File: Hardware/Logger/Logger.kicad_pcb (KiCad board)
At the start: 2 copper layers, 70 x 71 mm, 93 parts, among them CN1 Conn_02x19_Odd_Even, CN10 Conn_02x19_Odd_Even, CN2 Conn_02x19_Odd_Even, CN7 Conn_02x19_Odd_Even, J1 Conn_Coaxial, J10 Conn_01x08_Female, J2 Conn_Coaxial, J3 Conn_Coaxial, J4 Conn_Coaxial, J5 USB_B_Micro, J6 112K-TAA0-RA1_ATTEND, J7 DB9_Female_MountingHoles, J8 Conn_01x06_Female, J9 Conn_01x08_Female, Q1 FDV304P, Q2 FDV304P, Q3 FDV304P, Q4 FDV304P, Q5 BC848, Q6 BC848, Q7 BC848, Q8 BC848, SW1 SW_Push, SW2 SW_Push, SW3 SW_Push, SW4 SW_Push, U1 ESP-12E, U2 ST7735S, U3 LD1117ASTR

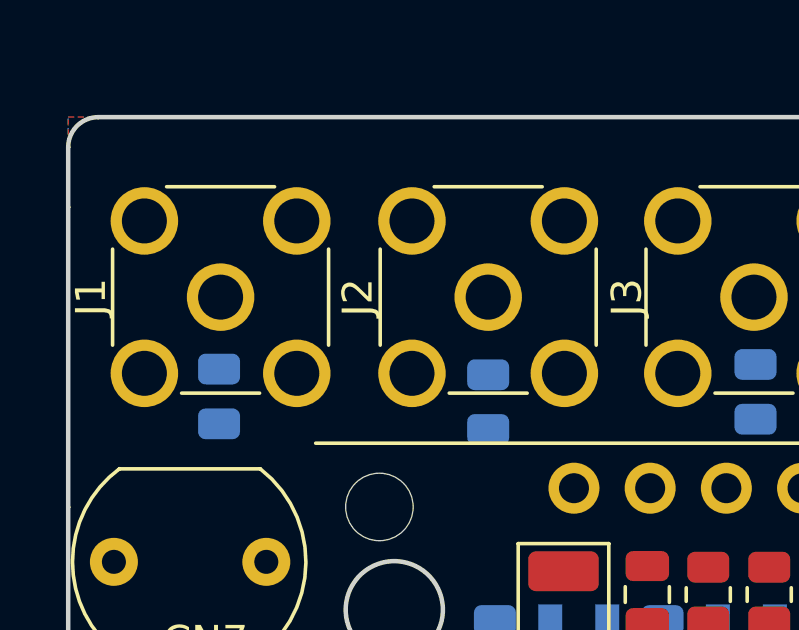
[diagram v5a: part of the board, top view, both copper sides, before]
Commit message: cleanup after transition to KiCad6
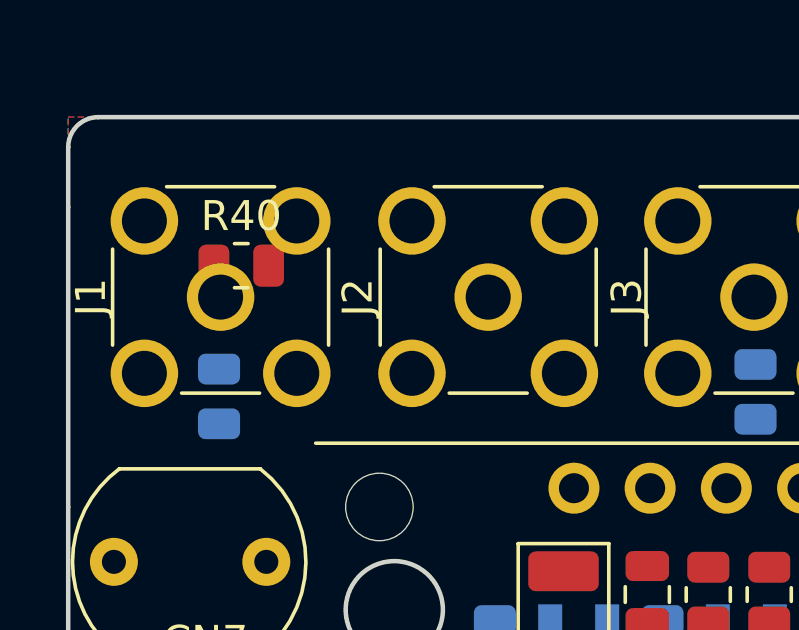
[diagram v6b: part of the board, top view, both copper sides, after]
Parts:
- removed the R10 at (144.0, 60.5)
- added R40: 100R, Resistor_SMD:R_0805_2012Metric, F.Cu at (135.8, 56.0)

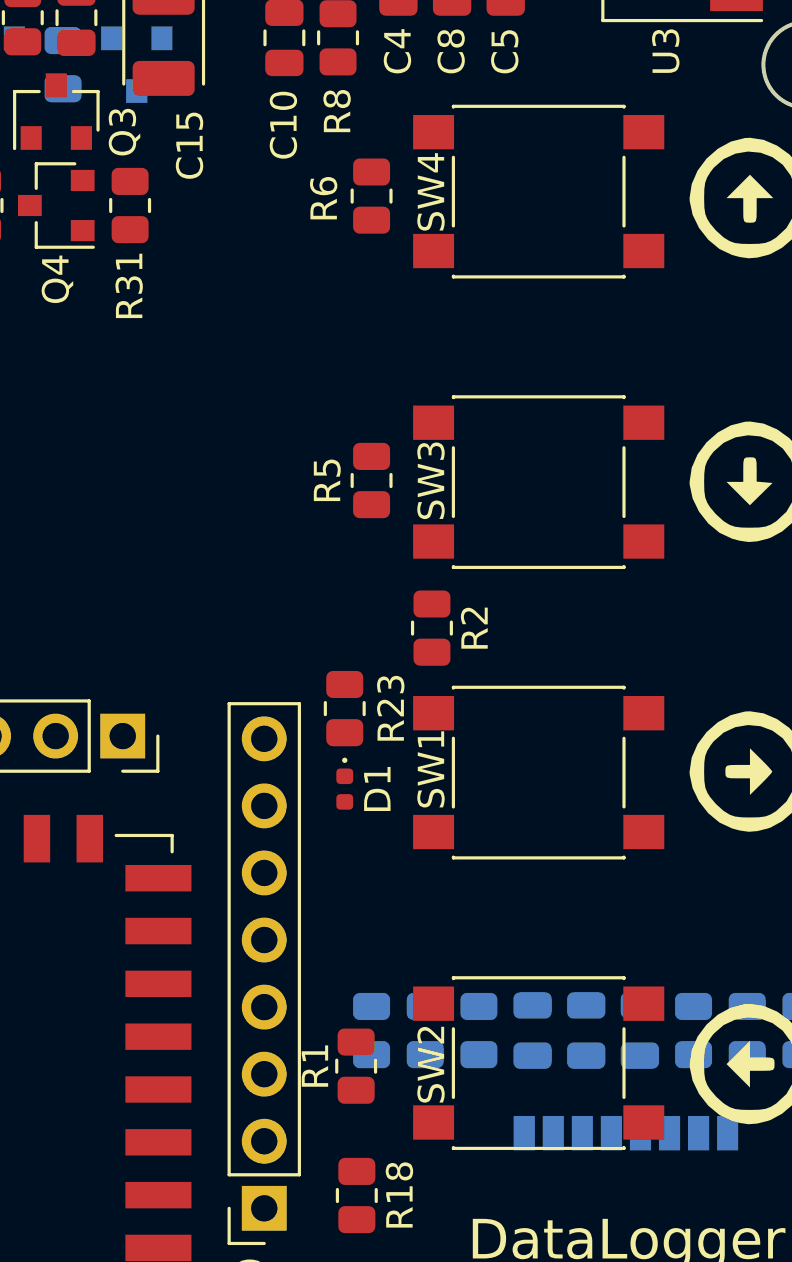
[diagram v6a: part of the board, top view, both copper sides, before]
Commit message: 1) LCD shows data but it's malformed; 2) fix #46
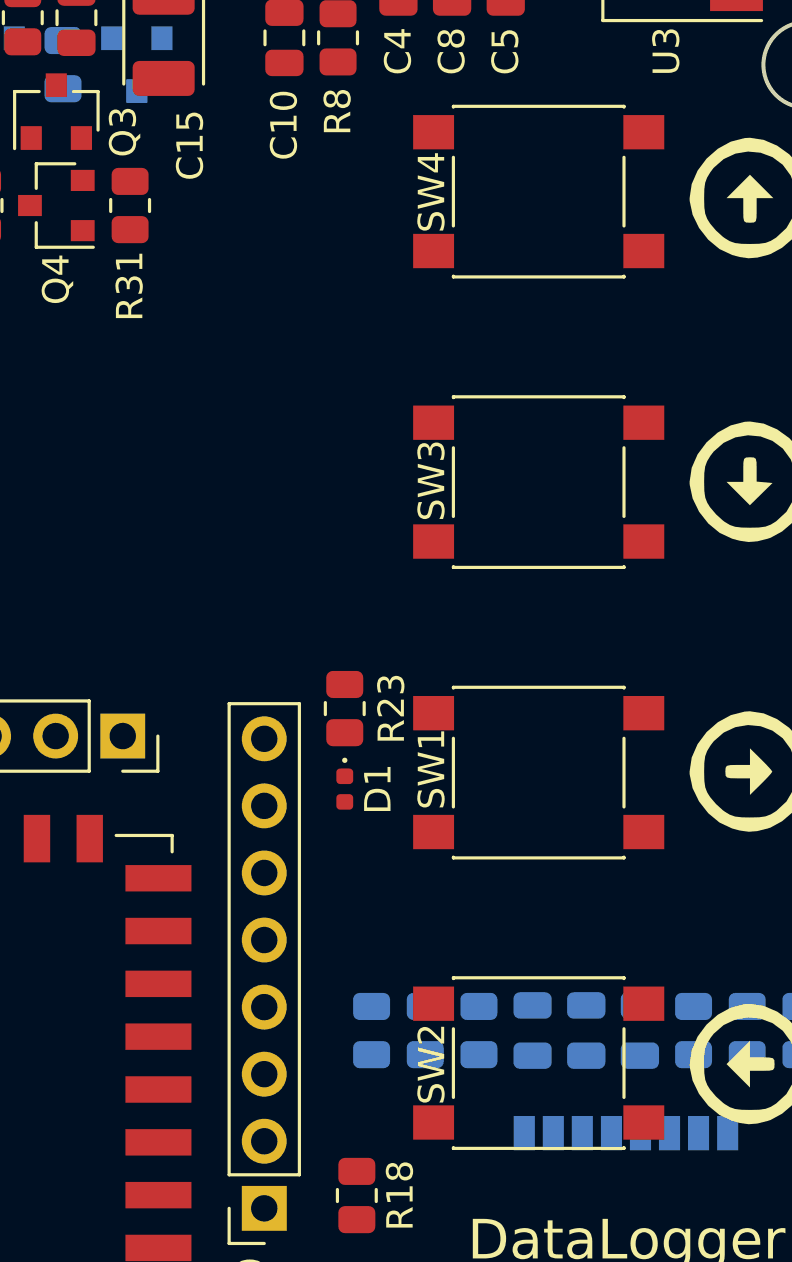
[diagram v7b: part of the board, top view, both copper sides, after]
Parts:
- removed R1, R2, R5, R6: 1k, Resistor_SMD:R_0805_2012Metric
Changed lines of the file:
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@@
-    )
-  )
-  (footprint "Resistor_SMD:R_0805_2012Metric" (layer "F.Cu")
-    (at 172.0878 106.6161 90)
-    (descr "Resistor SMD 0805 (2012 Metric), square (rectangular) end terminal, IPC_7351 nominal, (Body size source: IPC-SM-782 page 72, https://www.pcb-3d.com/wordpress/wp-content/uploads/ipc-sm-782a_amendment_1_and_2.pdf), generated with kicad-footprint-generator")
-    (tags "resistor")
-    (property "Sheetfile" "UserInterface.kicad_sch")
-    (property "Sheetname" "UserInterface")
-    (attr smd)
-    (fp_text reference "R1" (at 0 -1.524 90) (layer "F.SilkS")
-      (effects (font (size 1 1) (thickness 0.15)))
-    )
-    (fp_text value "1k" (at 0 1.65 90) (layer "F.Fab")
-      (effects (font (size 1 1) (thickness 0.15)))
-    )
-    (fp_text user "${REFERENCE}" (at 0 0 90) (layer "F.Fab")
-      (effects (font (size 0.5 0.5) (thickness 0.08)))
-    )
-    (fp_line (start -0.227064 0.735) (end 0.227064 0.735) (layer "F.SilkS") (width 0.12))
-    (fp_line (start -0.227064 -0.735) (end 0.227064 -0.735) (layer "F.SilkS") (width 0.12))
-    (fp_line (start -1.68 -0.95) (end 1.68 -0.95) (layer "F.CrtYd") (width 0.05))
-    (fp_line (start 1.68 0.95) (end -1.68 0.95) (layer "F.CrtYd") (width 0.05))
-    (fp_line (start -1.68 0.95) (end -1.68 -0.95) (layer "F.CrtYd") (width 0.05))
-    (fp_line (start 1.68 -0.95) (end 1.68 0.95) (layer "F.CrtYd") (width 0.05))
-    (fp_line (start 1 0.625) (end -1 0.625) (layer "F.Fab") (width 0.1))
-    (fp_line (start -1 -0.625) (end 1 -0.625) (layer "F.Fab") (width 0.1))
-    (fp_line (start -1 0.625) (end -1 -0.625) (layer "F.Fab") (width 0.1))
-    (fp_line (start 1 -0.625) (end 1 0.625) (layer "F.Fab") (width 0.1))
-    (pad "1" smd roundrect locked (at -0.9125 0 90) (size 1.025 1.4) (layers "F.Cu" "F.Paste" "F.Mask") (roundrect_rratio 0.243902)
-      (net 102 "3V3") (pintype "passive"))
-    (pad "2" smd roundrect locked (at 0.9125 0 90) (size 1.025 1.4) (layers "F.Cu" "F.Paste" "F.Mask") (roundrect_rratio 0.243902)
-      (net 77 "KEY_UP") (pintype "passive"))
-    (model "${KISYS3DMOD}/Resistor_SMD.3dshapes/R_0805_2012Metric.wrl"
-      (offset (xyz 0 0 0))
-      (scale (xyz 1 1 1))
-      (rotate (xyz 0 0 0))
-    )
-  )
-  (footprint "Resistor_SMD:R_0805_2012Metric" (layer "F.Cu")
-    (at 174.958 90.028 -90)
-    (descr "Resistor SMD 0805 (2012 Metric), square (rectangular) end terminal, IPC_7351 nominal, (Body size source: IPC-SM-782 page 72, https://www.pcb-3d.com/wordpress/wp-content/uploads/ipc-sm-782a_amendment_1_and_2.pdf), generated with kicad-footprint-generator")
-    (tags "resistor")
-    (property "Sheetfile" "UserInterface.kicad_sch")
-    (property "Sheetname" "UserInterface")
-    (attr smd)
-    (fp_text reference "R2" (at 0 -1.65 90) (layer "F.SilkS")
-      (effects (font (size 1 1) (thickness 0.15)))
-    )
-    (fp_text value "1k" (at 0 1.65 90) (layer "F.Fab")
-      (effects (font (size 1 1) (thickness 0.15)))
-    )
-    (fp_text user "${REFERENCE}" (at 0 0 90) (layer "F.Fab")
-      (effects (font (size 0.5 0.5) (thickness 0.08)))
-    )
-    (fp_line (start -0.227064 0.735) (end 0.227064 0.735) (layer "F.SilkS") (width 0.12))
-    (fp_line (start -0.227064 -0.735) (end 0.227064 -0.735) (layer "F.SilkS") (width 0.12))
-    (fp_line (start -1.68 -0.95) (end 1.68 -0.95) (layer "F.CrtYd") (width 0.05))
-    (fp_line (start 1.68 0.95) (end -1.68 0.95) (layer "F.CrtYd") (width 0.05))
-    (fp_line (start 1.68 -0.95) (end 1.68 0.95) (layer "F.CrtYd") (width 0.05))
-    (fp_line (start -1.68 0.95) (end -1.68 -0.95) (layer "F.CrtYd") (width 0.05))
-    (fp_line (start -1 -0.625) (end 1 -0.625) (layer "F.Fab") (width 0.1))
-    (fp_line (start 1 -0.625) (end 1 0.625) (layer "F.Fab") (width 0.1))
-    (fp_line (start -1 0.625) (end -1 -0.625) (layer "F.Fab") (width 0.1))
-    (fp_line (start 1 0.625) (end -1 0.625) (layer "F.Fab") (width 0.1))
-    (pad "1" smd roundrect locked (at -0.9125 0 270) (size 1.025 1.4) (layers "F.Cu" "F.Paste" "F.Mask") (roundrect_rratio 0.243902)
-      (net 102 "3V3") (pintype "passive"))
-    (pad "2" smd roundrect locked (at 0.9125 0 270) (size 1.025 1.4) (layers "F.Cu" "F.Paste" "F.Mask") (roundrect_rratio 0.243902)
-      (net 78 "KEY_DOWN") (pintype "passive"))
-    (model "${KISYS3DMOD}/Resistor_SMD.3dshapes/R_0805_2012Metric.wrl"
-      (offset (xyz 0 0 0))
-      (scale (xyz 1 1 1))
-      (rotate (xyz 0 0 0))
-    )
-  )
-  (footprint "Resistor_SMD:R_0805_2012Metric" (layer "F.Cu")
-    (at 172.672 84.44 90)
-    (descr "Resistor SMD 0805 (2012 Metric), square (rectangular) end terminal, IPC_7351 nominal, (Body size source: IPC-SM-782 page 72, https://www.pcb-3d.com/wordpress/wp-content/uploads/ipc-sm-782a_amendment_1_and_2.pdf), generated with kicad-footprint-generator")
-    (tags "resistor")
-    (property "Sheetfile" "UserInterface.kicad_sch")
-    (property "Sheetname" "UserInterface")
-    (attr smd)
-    (fp_text reference "R5" (at 0 -1.65 90) (layer "F.SilkS")
-      (effects (font (size 1 1) (thickness 0.15)))
-    )
-    (fp_text value "1k" (at 0 1.65 90) (layer "F.Fab")
-      (effects (font (size 1 1) (thickness 0.15)))
-    )
-    (fp_text user "${REFERENCE}" (at 0 0 90) (layer "F.Fab")
-      (effects (font (size 0.5 0.5) (thickness 0.08)))
-    )
-    (fp_line (start -0.227064 0.735) (end 0.227064 0.735) (layer "F.SilkS") (width 0.12))
-    (fp_line (start -0.227064 -0.735) (end 0.227064 -0.735) (layer "F.SilkS") (width 0.12))
-    (fp_line (start 1.68 -0.95) (end 1.68 0.95) (layer "F.CrtYd") (width 0.05))
-    (fp_line (start -1.68 -0.95) (end 1.68 -0.95) (layer "F.CrtYd") (width 0.05))
-    (fp_line (start -1.68 0.95) (end -1.68 -0.95) (layer "F.CrtYd") (width 0.05))
-    (fp_line (start 1.68 0.95) (end -1.68 0.95) (layer "F.CrtYd") (width 0.05))
-    (fp_line (start 1 0.625) (end -1 0.625) (layer "F.Fab") (width 0.1))
-    (fp_line (start 1 -0.625) (end 1 0.625) (layer "F.Fab") (width 0.1))
-    (fp_line (start -1 -0.625) (end 1 -0.625) (layer "F.Fab") (width 0.1))
-    (fp_line (start -1 0.625) (end -1 -0.625) (layer "F.Fab") (width 0.1))
-    (pad "1" smd roundrect locked (at -0.9125 0 90) (size 1.025 1.4) (layers "F.Cu" "F.Paste" "F.Mask") (roundrect_rratio 0.243902)
-      (net 102 "3V3") (pintype "passive"))
-    (pad "2" smd roundrect locked (at 0.9125 0 90) (size 1.025 1.4) (layers "F.Cu" "F.Paste" "F.Mask") (roundrect_rratio 0.243902)
-      (net 80 "KEY_LEFT") (pintype "passive"))
-    (model "${KISYS3DMOD}/Resistor_SMD.3dshapes/R_0805_2012Metric.wrl"
-      (offset (xyz 0 0 0))
-      (scale (xyz 1 1 1))
-      (rotate (xyz 0 0 0))
-    )
-  )
-  (footprint "Resistor_SMD:R_0805_2012Metric" (layer "F.Cu")
-    (at 172.672 73.6685 90)
-    (descr "Resistor SMD 0805 (2012 Metric), square (rectangular) end terminal, IPC_7351 nominal, (Body size source: IPC-SM-782 page 72, https://www.pcb-3d.com/wordpress/wp-content/uploads/ipc-sm-782a_amendment_1_and_2.pdf), generated with kicad-footprint-generator")
-    (tags "resistor")
-    (property "Sheetfile" "UserInterface.kicad_sch")
-    (property "Sheetname" "UserInterface")
-    (attr smd)
-    (fp_text reference "R6" (at -0.1035 -1.778 90) (layer "F.SilkS")
-      (effects (font (size 1 1) (thickness 0.15)))
-    )
-    (fp_text value "1k" (at 0 1.65 90) (layer "F.Fab")
-      (effects (font (size 1 1) (thickness 0.15)))
-    )
-    (fp_text user "${REFERENCE}" (at 0 0 90) (layer "F.Fab")
-      (effects (font (size 0.5 0.5) (thickness 0.08)))
-    )
-    (fp_line (start -0.227064 -0.735) (end 0.227064 -0.735) (layer "F.SilkS") (width 0.12))
-    (fp_line (start -0.227064 0.735) (end 0.227064 0.735) (layer "F.SilkS") (width 0.12))
-    (fp_line (start 1.68 -0.95) (end 1.68 0.95) (layer "F.CrtYd") (width 0.05))
-    (fp_line (start 1.68 0.95) (end -1.68 0.95) (layer "F.CrtYd") (width 0.05))
-    (fp_line (start -1.68 0.95) (end -1.68 -0.95) (layer "F.CrtYd") (width 0.05))
-    (fp_line (start -1.68 -0.95) (end 1.68 -0.95) (layer "F.CrtYd") (width 0.05))
-    (fp_line (start -1 0.625) (end -1 -0.625) (layer "F.Fab") (width 0.1))
-    (fp_line (start 1 0.625) (end -1 0.625) (layer "F.Fab") (width 0.1))
-    (fp_line (start 1 -0.625) (end 1 0.625) (layer "F.Fab") (width 0.1))
-    (fp_line (start -1 -0.625) (end 1 -0.625) (layer "F.Fab") (width 0.1))
-    (pad "1" smd roundrect locked (at -0.9125 0 90) (size 1.025 1.4) (layers "F.Cu" "F.Paste" "F.Mask") (roundrect_rratio 0.243902)
-      (net 102 "3V3") (pintype "passive"))
-    (pad "2" smd roundrect locked (at 0.9125 0 90) (size 1.025 1.4) (layers "F.Cu" "F.Paste" "F.Mask") (roundrect_rratio 0.243902)
-      (net 81 "KEY_RIGHT") (pintype "passive"))
-    (model "${KISYS3DMOD}/Resistor_SMD.3dshapes/R_0805_2012Metric.wrl"
-      (offset (xyz 0 0 0))
-      (scale (xyz 1 1 1))
-      (rotate (xyz 0 0 0))
     )
   )
